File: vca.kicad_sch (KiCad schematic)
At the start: 14 parts, among them Q1 BC309C, U6 CA3080, U7 LM741

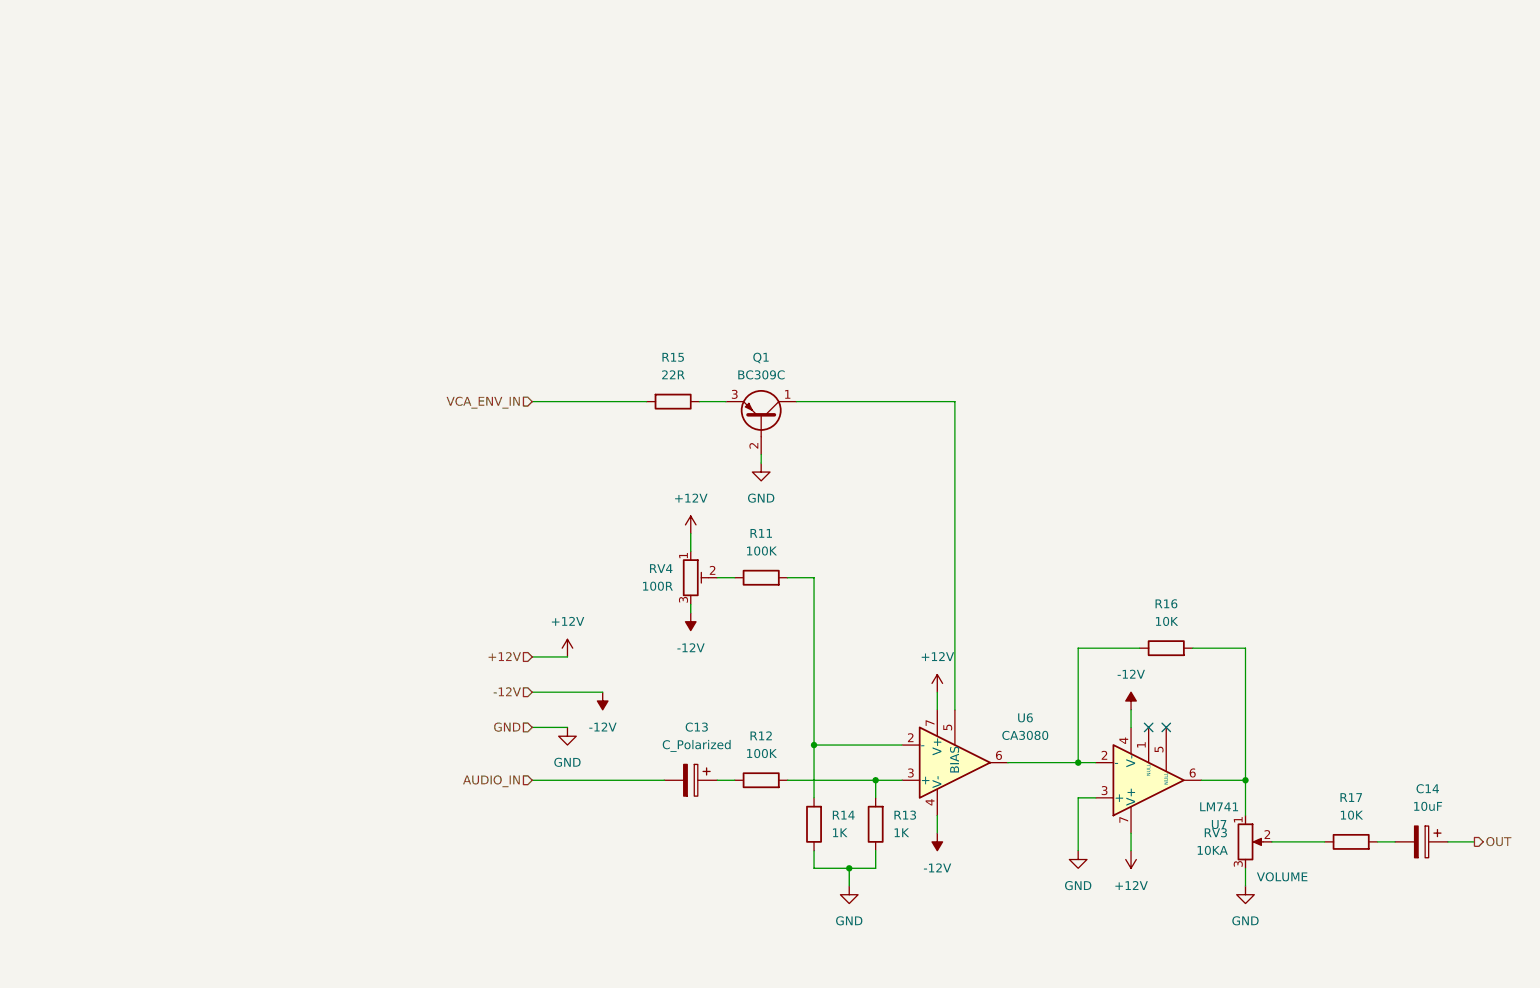
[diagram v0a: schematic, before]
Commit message: Add missing values and connectors
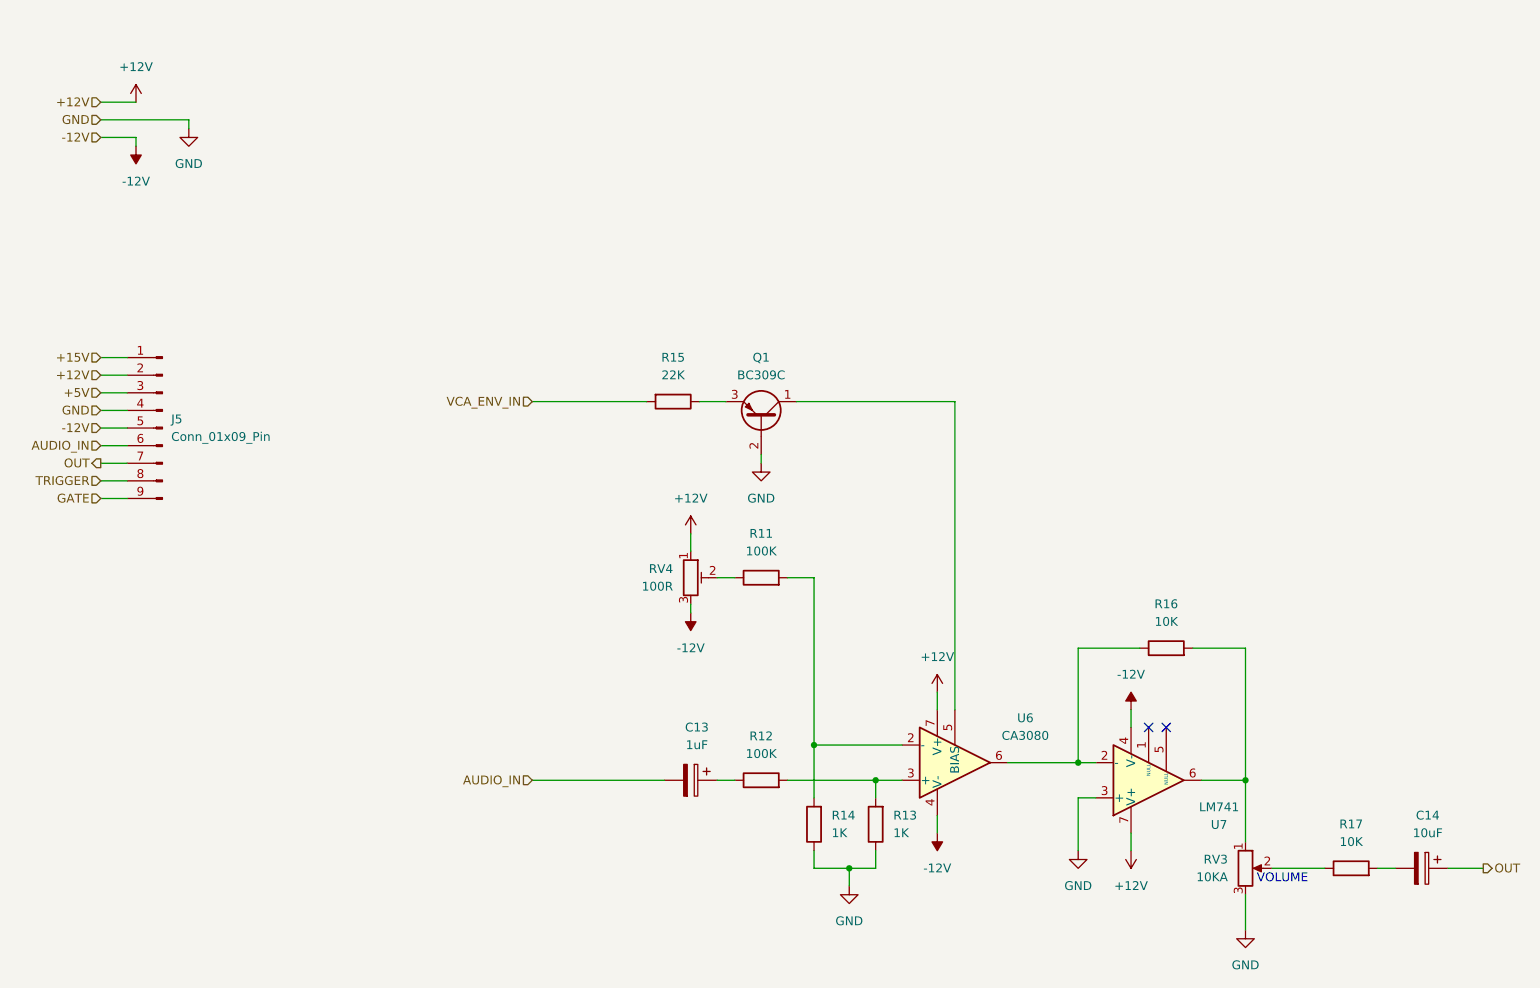
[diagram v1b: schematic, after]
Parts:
- added J5: Conn_01x09_Pin, symbol Connector:Conn_01x09_Pin
- C13: value C_Polarized -> 1uF
- R15: value 22R -> 22K
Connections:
- net +12V: now also J5.2 (Pin_2)
- net -12V: now also J5.5 (Pin_5)
- net AUDIO_IN: now also J5.6 (Pin_6)
- net GND: now also J5.4 (Pin_4)
- net OUT: now also J5.7 (Pin_7)
- new net +15V: J5.1 (Pin_1)
- new net +5V: J5.3 (Pin_3)
- new net GATE: J5.9 (Pin_9)
- new net TRIGGER: J5.8 (Pin_8)
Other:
- moved on the sheet: C14, R17, RV3

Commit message: Assign footprints and start PCB
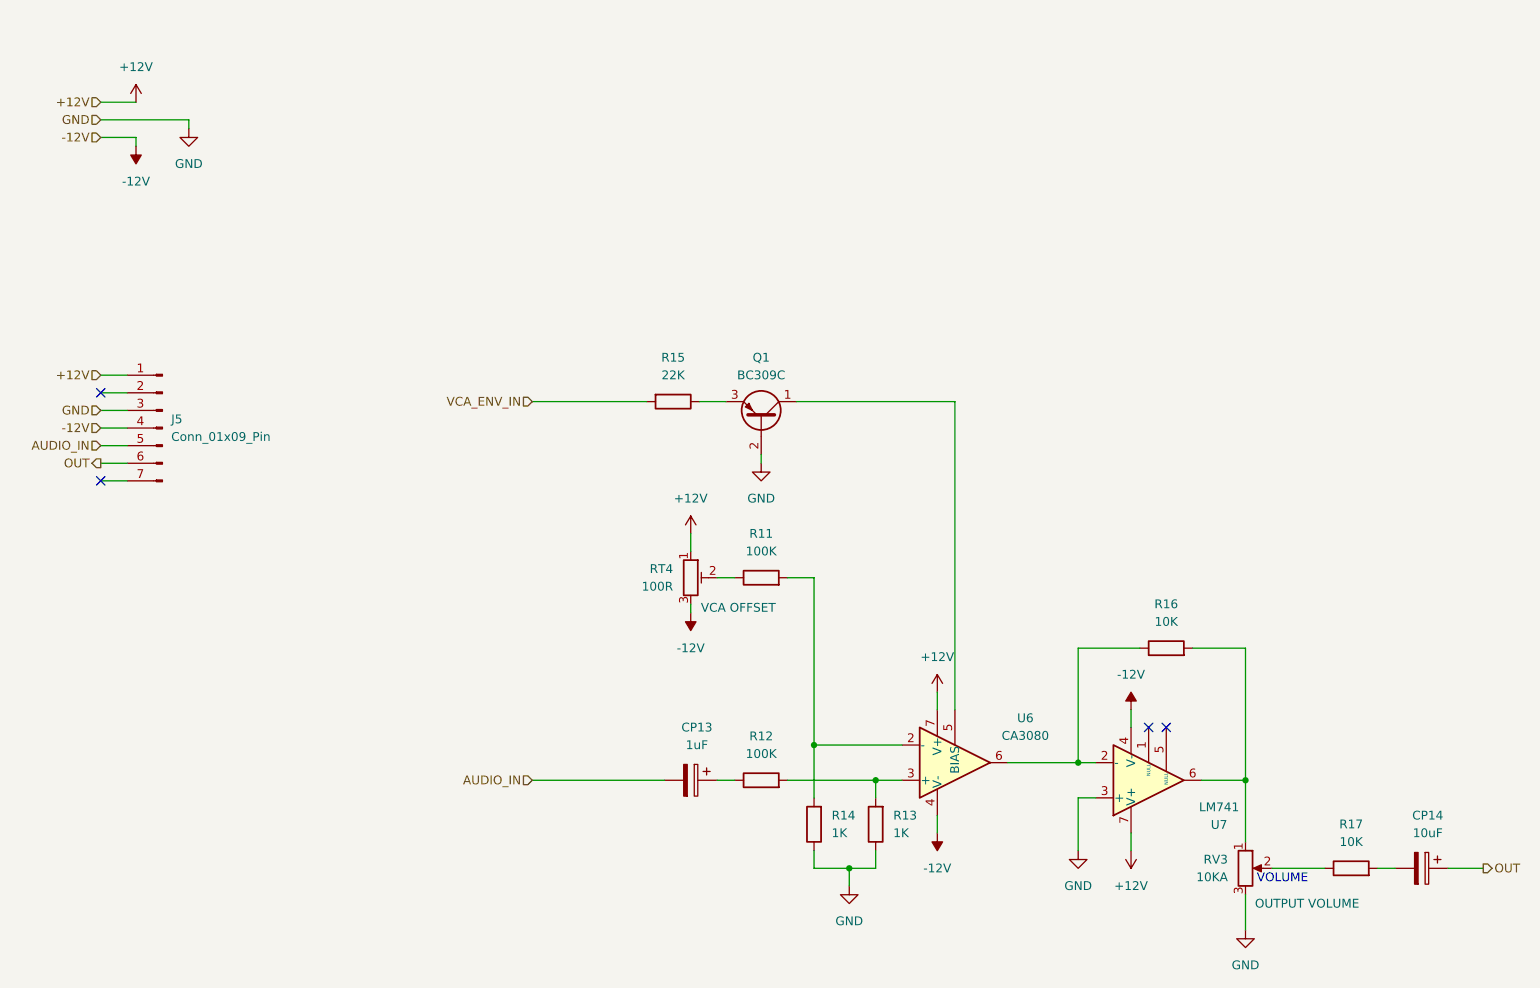
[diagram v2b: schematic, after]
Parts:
- CP13: renamed from C13; footprint (none) -> Capacitor_THT:CP_Radial_D8.0mm_P3.80mm
- CP14: renamed from C14; footprint (none) -> Capacitor_THT:CP_Radial_D8.0mm_P3.80mm
- J5: footprint (none) -> Connector_PinHeader_2.54mm:PinHeader_1x09_P2.54mm_Vertical; symbol Connector:Conn_01x09_Pin -> Connector:Conn_01x07_Pin
- R11, R12, R13, R14, R15, R16, R17: footprint (none) -> Resistor_THT:R_Axial_DIN0204_L3.6mm_D1.6mm_P7.62mm_Horizontal
- RT4: renamed from RV4; footprint (none) -> Potentiometer_THT:Potentiometer_Bourns_3339P_Vertical_HandSoldering
- RV3: footprint (none) -> Potentiometer_THT:Potentiometer_Omeg_PC16BU_Vertical
- U6, U7: footprint (none) -> Package_DIP:DIP-8_W7.62mm_LongPads
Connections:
- net +15V is gone; now on net +12V: J5.1 (Pin_1)
- net +5V is gone; now on net GND: J5.3 (Pin_3)
- net +12V: no longer J5.2 (Pin_2)
- net -12V: now also J5.4 (Pin_4); no longer J5.5 (Pin_5)
- net AUDIO_IN: now also J5.5 (Pin_5); no longer J5.6 (Pin_6)
- net GND: no longer J5.4 (Pin_4)
- net OUT: now also J5.6 (Pin_6); no longer J5.7 (Pin_7)
- removed net GATE: J5.9 (Pin_9)
- removed net TRIGGER: J5.8 (Pin_8)
- no-connect marks 2 -> 4
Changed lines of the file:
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@@
+	)
+	(no_connect
+		(at 26.67 66.04)
+	)
+	(no_connect
+		(at 26.67 78.74)
 	)
 	(no_connect
@@
 	(wire
 		(pts
-			(xy 26.67 81.28) (xy 30.48 81.28)
-		)
-		(stroke
-			(width 0)
-			(type default)
-		)
-	)
-	(wire
-		(pts
 			(xy 170.18 124.46) (xy 167.64 124.46)
 		)
@@
 		(pts
 			(xy 26.67 63.5) (xy 30.48 63.5)
-		)
-		(stroke
-			(width 0)
-			(type default)
-		)
-	)
-	(wire
-		(pts
-			(xy 26.67 60.96) (xy 30.48 60.96)
 		)
 		(stroke
@@
 		)
 	)
-	(hierarchical_label "GATE"
-		(shape input)
-		(at 26.67 81.28 180)
-		(effects
-			(font
-				(size 1.27 1.27)
-			)
-			(justify right)
-		)
-	)
 	(hierarchical_label "-12V"
 		(shape input)
@@
 		)
 	)
-	(hierarchical_label "TRIGGER"
-		(shape input)
-		(at 26.67 78.74 180)
-		(effects
-			(font
-				(size 1.27 1.27)
-			)
-			(justify right)
-		)
-	)
 	(hierarchical_label "AUDIO_IN"
 		(shape input)
@@
 		)
 	)
-	(hierarchical_label "+5V"
-		(shape input)
-		(at 26.67 66.04 180)
-		(effects
-			(font
-				(size 1.27 1.27)
-			)
-			(justify right)
-		)
-	)
 	(hierarchical_label "OUT"
 		(shape output)
@@
 		)
 	)
-	(hierarchical_label "+15V"
-		(shape input)
-		(at 26.67 60.96 180)
-		(effects
-			(font
-				(size 1.27 1.27)
-			)
-			(justify right)
-		)
-	)
 	(hierarchical_label "-12V"
 		(shape input)
@@
 		(on_board yes)
 		(dnp no)
-		(fields_autoplaced yes)
 		(property "Reference" "RV3"
 			(at 189.23 133.3499 0)
@@
 			)
 		)
-		(property "Footprint" ""
+		(property "Footprint" "Potentiometer_THT:Potentiometer_Omeg_PC16BU_Vertical"
 			(at 191.77 134.62 0)
 			(effects
@@
 			)
 		)
-		(property "Description" "Potentiometer"
-			(at 191.77 134.62 0)
-			(effects
-				(font
-					(size 1.27 1.27)
-				)
-				(hide yes)
+		(property "Description" "OUTPUT VOLUME"
+			(at 200.66 139.7 0)
+			(effects
+				(font
+					(size 1.27 1.27)
+				)
 			)
 		)
@@
 		(dnp no)
 		(fields_autoplaced yes)
-		(property "Reference" "C14"
+		(property "Reference" "CP14"
 			(at 218.059 127 90)
 			(effects
@@
 			)
 		)
-		(property "Footprint" ""
+		(property "Footprint" "Capacitor_THT:CP_Radial_D8.0mm_P3.80mm"
 			(at 213.36 135.5852 0)
 			(effects
@@
 			(project "jensx1000"
 				(path "/3c53febc-5769-4c45-8f8f-0aba2c04e944/75668585-e3c2-431b-bb9e-906e88891a90"
-					(reference "C14")
+					(reference "CP14")
 					(unit 1)
 				)
@@
 			)
 		)
-		(property "Footprint" ""
+		(property "Footprint" "Resistor_THT:R_Axial_DIN0204_L3.6mm_D1.6mm_P7.62mm_Horizontal"
 			(at 180.34 104.648 90)
 			(effects
@@
 			)
 		)
-		(property "Footprint" ""
+		(property "Footprint" "Resistor_THT:R_Axial_DIN0204_L3.6mm_D1.6mm_P7.62mm_Horizontal"
 			(at 121.92 94.488 90)
 			(effects
@@
 			)
 		)
-		(property "Footprint" ""
+		(property "Footprint" "Resistor_THT:R_Axial_DIN0204_L3.6mm_D1.6mm_P7.62mm_Horizontal"
 			(at 109.22 65.532 90)
 			(effects
@@
 			)
 		)
-		(property "Footprint" ""
+		(property "Footprint" "Resistor_THT:R_Axial_DIN0204_L3.6mm_D1.6mm_P7.62mm_Horizontal"
 			(at 131.318 128.27 90)
 			(effects
@@
 	)
 	(symbol
-		(lib_id "Connector:Conn_01x09_Pin")
+		(lib_id "Connector:Conn_01x07_Pin")
 		(at 35.56 71.12 0)
 		(mirror y)
@@
 			)
 		)
-		(property "Footprint" ""
+		(property "Footprint" "Connector_PinHeader_2.54mm:PinHeader_1x09_P2.54mm_Vertical"
 			(at 35.56 71.12 0)
 			(effects
@@
 			)
 		)
-		(property "Description" "Generic connector, single row, 01x09, script generated"
+		(property "Description" "Generic connector, single row, 01x07, script generated"
 			(at 35.56 71.12 0)
 			(effects
@@
 		)
 		(pin "7"
-		)
-		(pin "8"
-		)
-		(pin "9"
 		)
 		(instances
@@
 		(dnp no)
 		(fields_autoplaced yes)
-		(property "Reference" "C13"
+		(property "Reference" "CP13"
 			(at 112.649 114.3 90)
 			(effects
@@
 			)
 		)
-		(property "Footprint" ""
+		(property "Footprint" "Capacitor_THT:CP_Radial_D8.0mm_P3.80mm"
 			(at 107.95 122.8852 0)
 			(effects
@@
 			(project ""
 				(path "/3c53febc-5769-4c45-8f8f-0aba2c04e944/75668585-e3c2-431b-bb9e-906e88891a90"
-					(reference "C13")
+					(reference "CP13")
 					(unit 1)
 				)
@@
 			)
 		)
-		(property "Footprint" ""
+		(property "Footprint" "Package_DIP:DIP-8_W7.62mm_LongPads"
 			(at 149.86 119.38 0)
 			(effects
@@
 			)
 		)
-		(property "Footprint" ""
+		(property "Footprint" "Package_DIP:DIP-8_W7.62mm_LongPads"
 			(at 179.07 123.19 0)
 			(effects
@@
 		(on_board yes)
 		(dnp no)
-		(fields_autoplaced yes)
-		(property "Reference" "RV4"
+		(property "Reference" "RT4"
 			(at 109.22 91.4399 0)
 			(effects
@@
 			)
 		)
-		(property "Footprint" ""
+		(property "Footprint" "Potentiometer_THT:Potentiometer_Bourns_3339P_Vertical_HandSoldering"
 			(at 111.76 92.71 0)
 			(effects
@@
 			)
 		)
-		(property "Description" "Trim-potentiometer"
-			(at 111.76 92.71 0)
-			(effects
-				(font
-					(size 1.27 1.27)
-				)
-				(hide yes)
+		(property "Description" "VCA OFFSET"
+			(at 118.618 97.028 0)
+			(effects
+				(font
+					(size 1.27 1.27)
+				)
 			)
 		)
@@
 			(project ""
 				(path "/3c53febc-5769-4c45-8f8f-0aba2c04e944/75668585-e3c2-431b-bb9e-906e88891a90"
-					(reference "RV4")
+					(reference "RT4")
 					(unit 1)
 				)
@@
 			)
 		)
-		(property "Footprint" ""
+		(property "Footprint" "Resistor_THT:R_Axial_DIN0204_L3.6mm_D1.6mm_P7.62mm_Horizontal"
 			(at 207.01 136.398 90)
 			(effects
@@
 			)
 		)
-		(property "Footprint" ""
+		(property "Footprint" "Resistor_THT:R_Axial_DIN0204_L3.6mm_D1.6mm_P7.62mm_Horizontal"
 			(at 140.208 128.27 90)
 			(effects
@@
 			)
 		)
-		(property "Footprint" ""
+		(property "Footprint" "Resistor_THT:R_Axial_DIN0204_L3.6mm_D1.6mm_P7.62mm_Horizontal"
 			(at 121.92 123.698 90)
 			(effects

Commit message: VCO components are in position
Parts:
- Q1: footprint Package_TO_SOT_THT:TO-92_Inline -> Package_TO_SOT_THT:TO-92_Inline_Wide
- R11, R13, R14: footprint Resistor_THT:R_Axial_DIN0204_L3.6mm_D1.6mm_P7.62mm_Horizontal -> Resistor_THT:R_Axial_DIN0309_L9.0mm_D3.2mm_P12.70mm_Horizontal
- R12, R15, R16, R17: footprint Resistor_THT:R_Axial_DIN0204_L3.6mm_D1.6mm_P7.62mm_Horizontal -> Resistor_THT:R_Axial_DIN0207_L6.3mm_D2.5mm_P15.24mm_Horizontal
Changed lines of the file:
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@@
 			)
 		)
-		(property "Footprint" "Resistor_THT:R_Axial_DIN0204_L3.6mm_D1.6mm_P7.62mm_Horizontal"
+		(property "Footprint" "Resistor_THT:R_Axial_DIN0207_L6.3mm_D2.5mm_P15.24mm_Horizontal"
 			(at 180.34 104.648 90)
 			(effects
@@
 			)
 		)
-		(property "Footprint" "Resistor_THT:R_Axial_DIN0204_L3.6mm_D1.6mm_P7.62mm_Horizontal"
+		(property "Footprint" "Resistor_THT:R_Axial_DIN0309_L9.0mm_D3.2mm_P12.70mm_Horizontal"
 			(at 121.92 94.488 90)
 			(effects
@@
 			)
 		)
-		(property "Footprint" "Resistor_THT:R_Axial_DIN0204_L3.6mm_D1.6mm_P7.62mm_Horizontal"
+		(property "Footprint" "Resistor_THT:R_Axial_DIN0207_L6.3mm_D2.5mm_P15.24mm_Horizontal"
 			(at 109.22 65.532 90)
 			(effects
@@
 			)
 		)
-		(property "Footprint" "Package_TO_SOT_THT:TO-92_Inline"
+		(property "Footprint" "Package_TO_SOT_THT:TO-92_Inline_Wide"
 			(at 120.015 64.77 0)
 			(effects
@@
 			)
 		)
-		(property "Footprint" "Resistor_THT:R_Axial_DIN0204_L3.6mm_D1.6mm_P7.62mm_Horizontal"
+		(property "Footprint" "Resistor_THT:R_Axial_DIN0309_L9.0mm_D3.2mm_P12.70mm_Horizontal"
 			(at 131.318 128.27 90)
 			(effects
@@
 			)
 		)
-		(property "Footprint" "Resistor_THT:R_Axial_DIN0204_L3.6mm_D1.6mm_P7.62mm_Horizontal"
+		(property "Footprint" "Resistor_THT:R_Axial_DIN0207_L6.3mm_D2.5mm_P15.24mm_Horizontal"
 			(at 207.01 136.398 90)
 			(effects
@@
 			)
 		)
-		(property "Footprint" "Resistor_THT:R_Axial_DIN0204_L3.6mm_D1.6mm_P7.62mm_Horizontal"
+		(property "Footprint" "Resistor_THT:R_Axial_DIN0309_L9.0mm_D3.2mm_P12.70mm_Horizontal"
 			(at 140.208 128.27 90)
 			(effects
@@
 			)
 		)
-		(property "Footprint" "Resistor_THT:R_Axial_DIN0204_L3.6mm_D1.6mm_P7.62mm_Horizontal"
+		(property "Footprint" "Resistor_THT:R_Axial_DIN0207_L6.3mm_D2.5mm_P15.24mm_Horizontal"
 			(at 121.92 123.698 90)
 			(effects

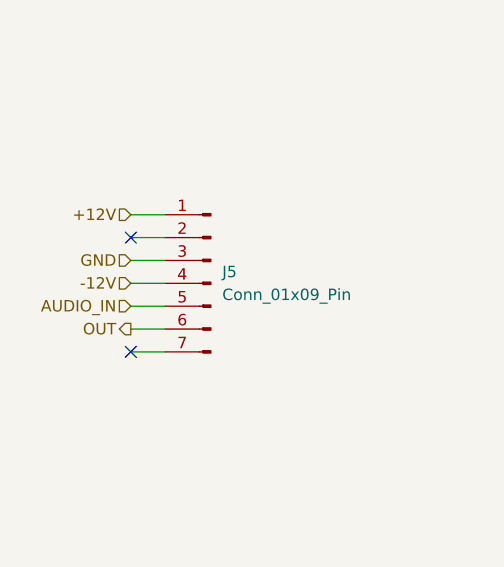
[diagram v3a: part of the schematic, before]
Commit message: Fix PCB sizes, adjust layout to new size
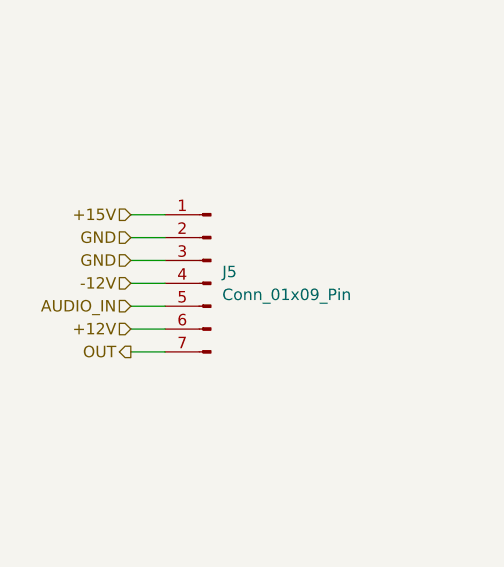
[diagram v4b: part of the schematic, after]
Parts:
- J5: footprint Connector_PinHeader_2.54mm:PinHeader_1x09_P2.54mm_Vertical -> Connector_PinHeader_2.54mm:PinHeader_1x07_P2.54mm_Vertical
- RT4: footprint Potentiometer_THT:Potentiometer_Bourns_3339P_Vertical_HandSoldering -> Potentiometer_THT:Potentiometer_Piher_PT-10-V10_Vertical
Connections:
- net +12V: now also J5.6 (Pin_6); no longer J5.1 (Pin_1)
- net GND: now also J5.2 (Pin_2)
- net OUT: now also J5.7 (Pin_7); no longer J5.6 (Pin_6)
- new net +15V: J5.1 (Pin_1)
- no-connect marks 4 -> 2
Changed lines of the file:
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@@
-	)
-	(no_connect
-		(at 26.67 66.04)
-	)
-	(no_connect
-		(at 26.67 78.74)
 	)
 	(no_connect
@@
 		)
 	)
+	(hierarchical_label "+15V"
+		(shape input)
+		(at 26.67 63.5 180)
+		(effects
+			(font
+				(size 1.27 1.27)
+			)
+			(justify right)
+		)
+	)
 	(hierarchical_label "-12V"
 		(shape input)
@@
 	(hierarchical_label "OUT"
 		(shape output)
-		(at 26.67 76.2 180)
+		(at 26.67 78.74 180)
 		(effects
 			(font
@@
 	(hierarchical_label "+12V"
 		(shape input)
-		(at 26.67 63.5 180)
+		(at 26.67 76.2 180)
 		(effects
 			(font
@@
 		)
 	)
+	(hierarchical_label "GND"
+		(shape input)
+		(at 26.67 66.04 180)
+		(effects
+			(font
+				(size 1.27 1.27)
+			)
+			(justify right)
+		)
+	)
 	(hierarchical_label "OUT"
 		(shape output)
@@
 			)
 		)
-		(property "Footprint" "Connector_PinHeader_2.54mm:PinHeader_1x09_P2.54mm_Vertical"
+		(property "Footprint" "Connector_PinHeader_2.54mm:PinHeader_1x07_P2.54mm_Vertical"
 			(at 35.56 71.12 0)
 			(effects
@@
 			)
 		)
-		(property "Footprint" "Potentiometer_THT:Potentiometer_Bourns_3339P_Vertical_HandSoldering"
+		(property "Footprint" "Potentiometer_THT:Potentiometer_Piher_PT-10-V10_Vertical"
 			(at 111.76 92.71 0)
 			(effects
